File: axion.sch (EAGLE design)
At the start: 148 parts, among them IC1 3.3V, IC2 5V, Q2 12.288Mhz, U10 MIC2039, U11 WM8731, U2 Intel Edison, U4 FT232RLSSOP, U5 PCA9306D, U6 74HC4050, U7 TPA2005D1DGN, X1 MKDSN1,5/2-5,08, X2 ZX62R-AB-5P, X3 ST-005-G, X4 ZX62R-B-5P

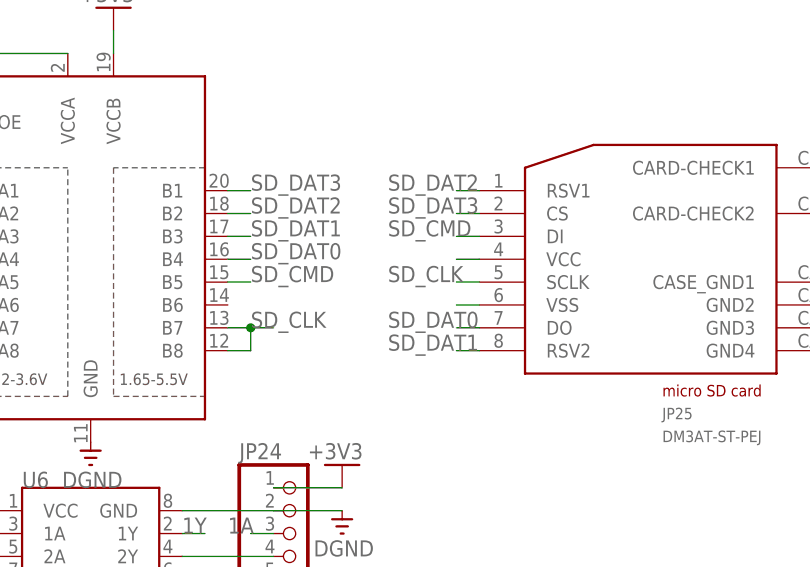
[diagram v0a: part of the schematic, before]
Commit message: Power microSD
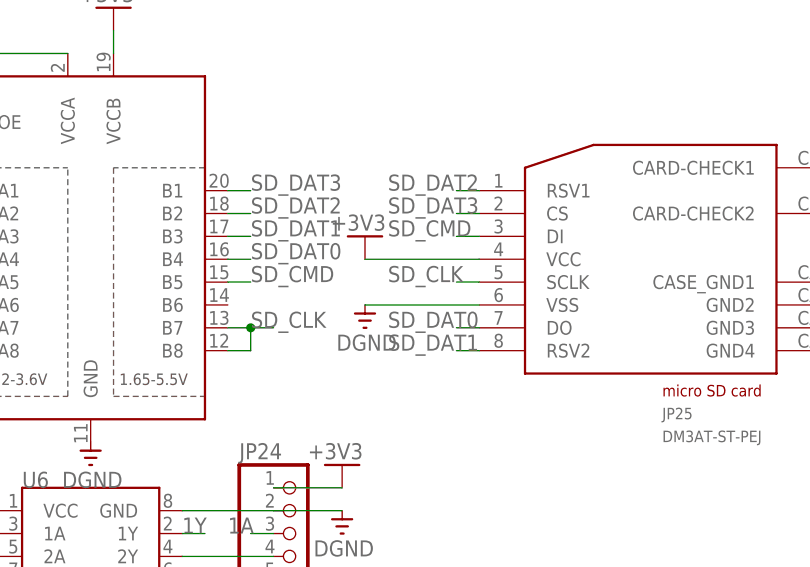
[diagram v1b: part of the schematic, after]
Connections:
- removed net N$49: JP25.VCC
- removed net N$51: JP25.VSS
- net +3V3: now also JP25.VCC
- net DGND: now also JP25.VSS
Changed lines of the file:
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@@
 </part>
 <part name="X4" library="hirose-zx" deviceset="ZX62R-B-5P" device=""/>
+<part name="DGND34" library="supply0" deviceset="DGND" device=""/>
+<part name="V43" library="supply0" deviceset="+3V3" device=""/>
 </parts>
 <sheets>
@@
 <instance part="X4" gate="C" x="-119.38" y="20.32" rot="MR0"/>
 <instance part="X4" gate="S" x="-124.46" y="10.16" rot="MR0"/>
+<instance part="DGND34" gate="G$1" x="78.74" y="-17.78"/>
+<instance part="V43" gate="G$1" x="78.74" y="-7.62"/>
 </instances>
 <busses>
@@
 <pinref part="DGND26" gate="G$1" pin="DGND"/>
 </segment>
+<segment>
+<pinref part="JP25" gate="G$1" pin="VSS"/>
+<pinref part="DGND34" gate="G$1" pin="DGND"/>
+<wire x1="91.44" y1="-15.24" x2="78.74" y2="-15.24" width="0.1524" layer="91"/>
+</segment>
 </net>
 <net name="+3V3" class="2">
@@
 <wire x1="-111.76" y1="50.8" x2="-116.84" y2="50.8" width="0.1524" layer="91"/>
 </segment>
+<segment>
+<pinref part="JP25" gate="G$1" pin="VCC"/>
+<pinref part="V43" gate="G$1" pin="+3V3"/>
+<wire x1="78.74" y1="-10.16" x2="91.44" y2="-10.16" width="0.1524" layer="91"/>
+</segment>
 </net>
 <net name="+5V" class="2">
@@
 </segment>
 </net>
-<net name="N$49" class="0">
-<segment>
-<pinref part="JP25" gate="G$1" pin="VCC"/>
-<wire x1="91.44" y1="-10.16" x2="88.9" y2="-10.16" width="0.1524" layer="91"/>
-</segment>
-</net>
-<net name="N$51" class="0">
-<segment>
-<pinref part="JP25" gate="G$1" pin="VSS"/>
-<wire x1="91.44" y1="-15.24" x2="88.9" y2="-15.24" width="0.1524" layer="91"/>
-</segment>
-</net>

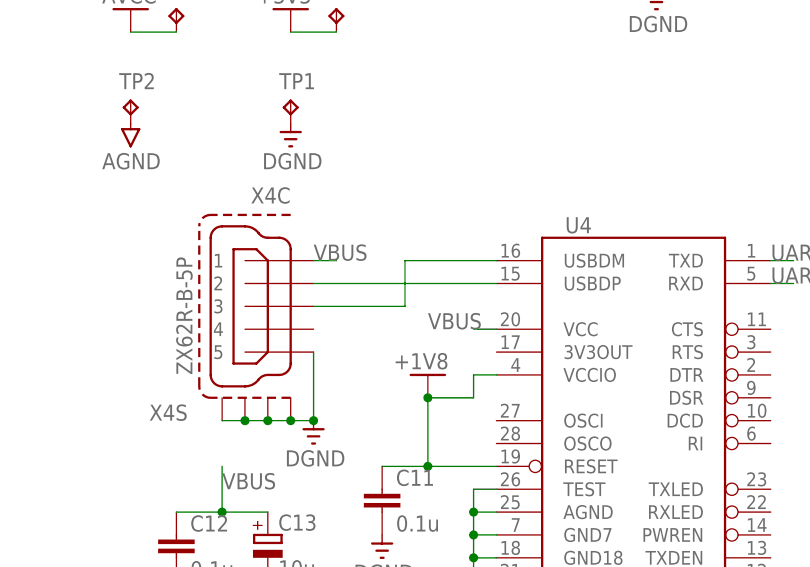
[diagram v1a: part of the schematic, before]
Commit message: Disconnect between USBD{P,M} of USB-serial bridge
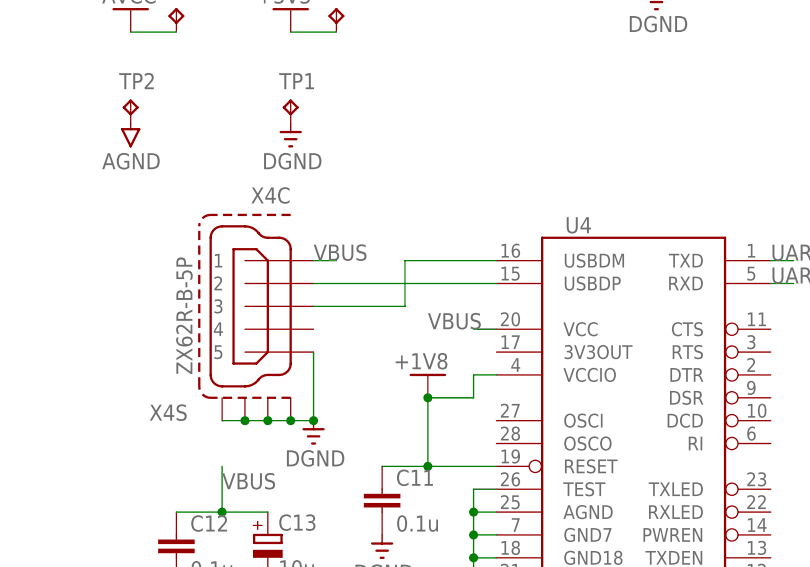
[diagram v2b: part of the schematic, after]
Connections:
- new net N$49: U4.USBDM, X4C.3
- net N$8: no longer U4.USBDM, X4C.3
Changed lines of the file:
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@@
-</segment>
-</net>
-<net name="N$8" class="0">
-<segment>
-<pinref part="U4" gate="G$1" pin="USBDP"/>
-<wire x1="-114.3" y1="22.86" x2="-104.14" y2="22.86" width="0.1524" layer="91"/>
-<wire x1="-104.14" y1="22.86" x2="-93.98" y2="22.86" width="0.1524" layer="91"/>
-<wire x1="-114.3" y1="20.32" x2="-104.14" y2="20.32" width="0.1524" layer="91"/>
-<wire x1="-104.14" y1="20.32" x2="-104.14" y2="22.86" width="0.1524" layer="91"/>
-<wire x1="-104.14" y1="22.86" x2="-104.14" y2="25.4" width="0.1524" layer="91"/>
-<pinref part="U4" gate="G$1" pin="USBDM"/>
-<wire x1="-104.14" y1="25.4" x2="-93.98" y2="25.4" width="0.1524" layer="91"/>
-<pinref part="X4" gate="C" pin="2"/>
-<pinref part="X4" gate="C" pin="3"/>
 </segment>
 </net>
@@
 </segment>
 </net>
+<net name="N$8" class="0">
+<segment>
+<pinref part="X4" gate="C" pin="2"/>
+<pinref part="U4" gate="G$1" pin="USBDP"/>
+<wire x1="-114.3" y1="22.86" x2="-93.98" y2="22.86" width="0.1524" layer="91"/>
+</segment>
+</net>
+<net name="N$49" class="0">
+<segment>
+<pinref part="U4" gate="G$1" pin="USBDM"/>
+<wire x1="-93.98" y1="25.4" x2="-104.14" y2="25.4" width="0.1524" layer="91"/>
+<wire x1="-104.14" y1="25.4" x2="-104.14" y2="20.32" width="0.1524" layer="91"/>
+<pinref part="X4" gate="C" pin="3"/>
+<wire x1="-104.14" y1="20.32" x2="-114.3" y2="20.32" width="0.1524" layer="91"/>
+</segment>
+</net>

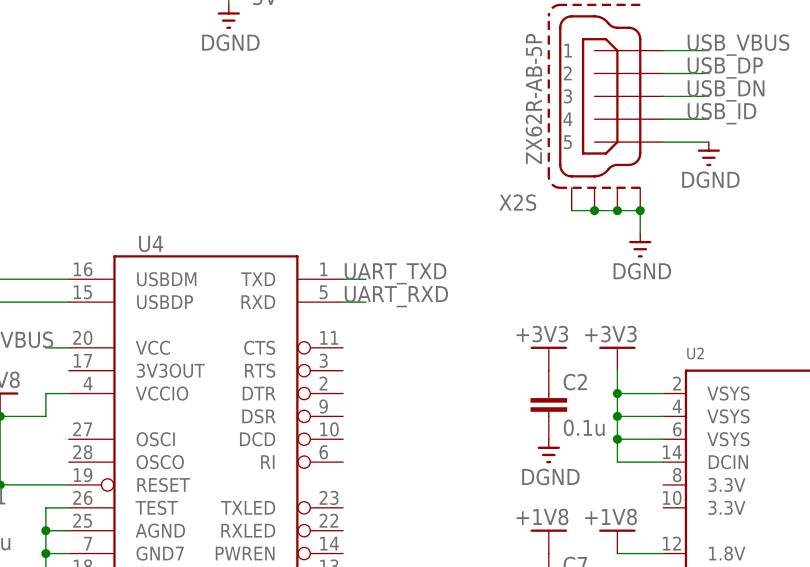
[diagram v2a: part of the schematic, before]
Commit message: Fix the order of {T,R}XD of serial
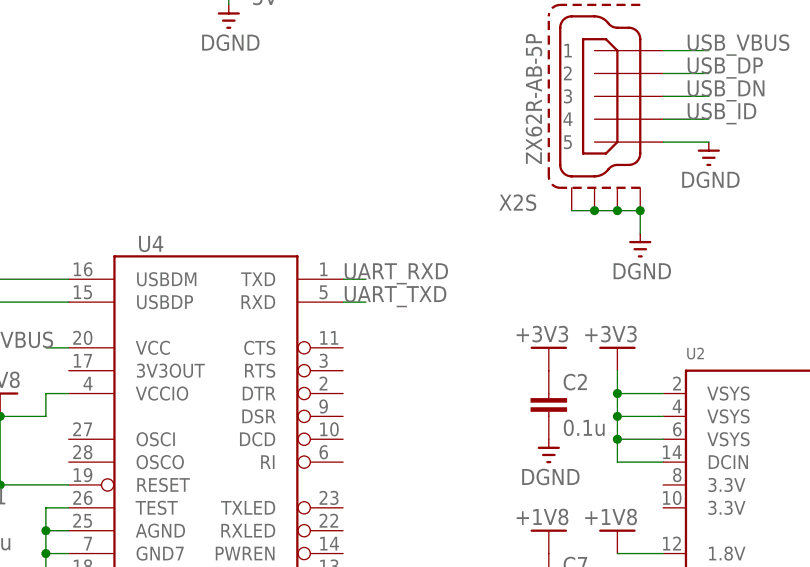
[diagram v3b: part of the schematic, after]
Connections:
- net UART_RXD: now also U4.TXD; no longer U4.RXD
- net UART_TXD: now also U4.RXD; no longer U4.TXD
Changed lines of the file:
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@@
 </segment>
 <segment>
-<pinref part="U4" gate="G$1" pin="TXD"/>
-<wire x1="-63.5" y1="25.4" x2="-60.96" y2="25.4" width="0.1524" layer="91"/>
-<label x="-63.5" y="25.4" size="1.778" layer="95"/>
+<pinref part="U4" gate="G$1" pin="RXD"/>
+<wire x1="-63.5" y1="22.86" x2="-60.96" y2="22.86" width="0.1524" layer="91"/>
+<label x="-63.5" y="22.86" size="1.778" layer="95"/>
 </segment>
 </net>
@@
 </segment>
 <segment>
-<pinref part="U4" gate="G$1" pin="RXD"/>
-<wire x1="-63.5" y1="22.86" x2="-60.96" y2="22.86" width="0.1524" layer="91"/>
-<label x="-63.5" y="22.86" size="1.778" layer="95"/>
+<pinref part="U4" gate="G$1" pin="TXD"/>
+<wire x1="-63.5" y1="25.4" x2="-60.96" y2="25.4" width="0.1524" layer="91"/>
+<label x="-63.5" y="25.4" size="1.778" layer="95"/>
 </segment>
 </net>

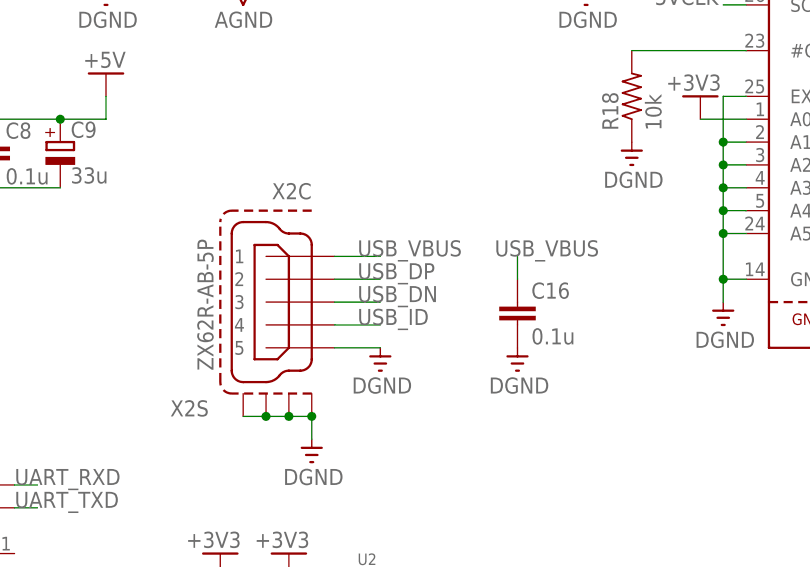
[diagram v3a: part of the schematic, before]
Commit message: Fix the order of USBD{P,M} od OTG USB
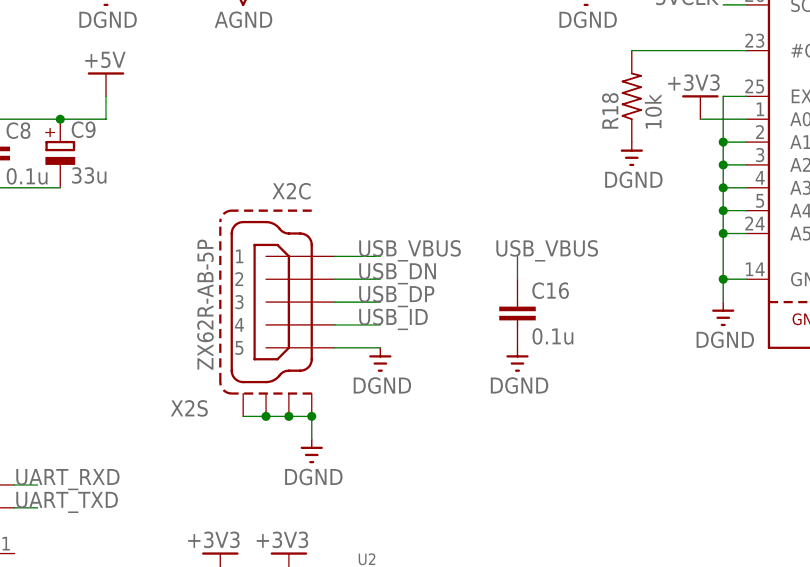
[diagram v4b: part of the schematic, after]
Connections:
- net USB_DN: now also X2C.2; no longer X2C.3
- net USB_DP: now also X2C.3; no longer X2C.2
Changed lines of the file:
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@@
 </segment>
 <segment>
-<wire x1="-27.94" y1="48.26" x2="-22.86" y2="48.26" width="0.1524" layer="91"/>
-<label x="-25.4" y="48.26" size="1.778" layer="95"/>
-<pinref part="X2" gate="C" pin="2"/>
+<wire x1="-27.94" y1="45.72" x2="-22.86" y2="45.72" width="0.1524" layer="91"/>
+<label x="-25.4" y="45.72" size="1.778" layer="95"/>
+<pinref part="X2" gate="C" pin="3"/>
 </segment>
 </net>
@@
 </segment>
 <segment>
-<wire x1="-27.94" y1="45.72" x2="-22.86" y2="45.72" width="0.1524" layer="91"/>
-<label x="-25.4" y="45.72" size="1.778" layer="95"/>
-<pinref part="X2" gate="C" pin="3"/>
+<wire x1="-27.94" y1="48.26" x2="-22.86" y2="48.26" width="0.1524" layer="91"/>
+<label x="-25.4" y="48.26" size="1.778" layer="95"/>
+<pinref part="X2" gate="C" pin="2"/>
 </segment>
 </net>

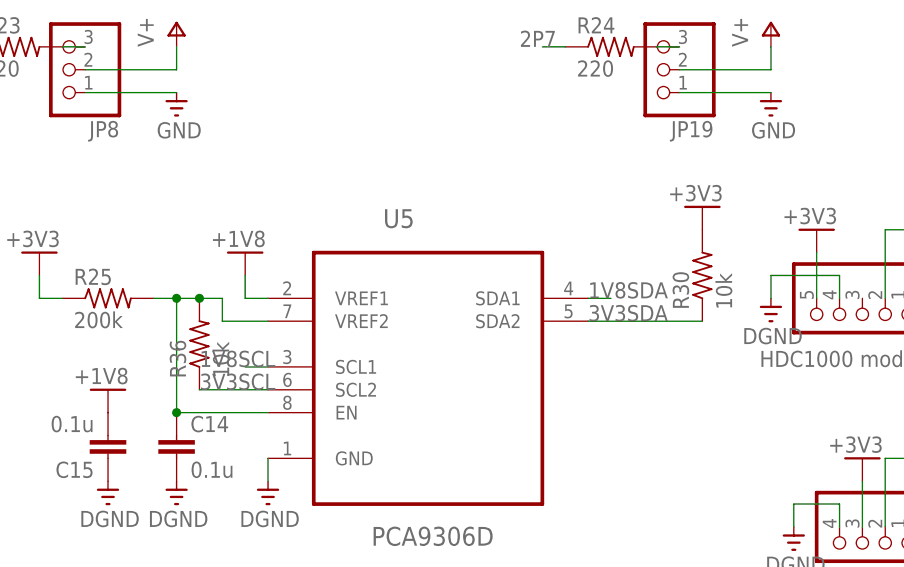
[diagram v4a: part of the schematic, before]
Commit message: Remove 10k pullup of I2C
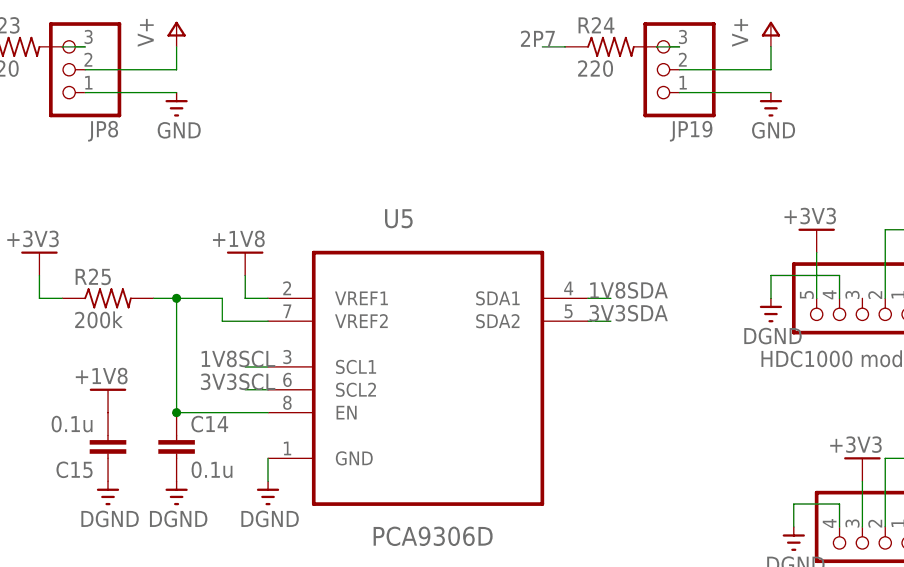
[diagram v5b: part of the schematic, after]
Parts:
- removed R30, R36: 10k, resistor:R-US_M1206
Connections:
- net +3V3: no longer R30.2
- net 3V3SCL: no longer R36.1
- net 3V3SDA: no longer R30.1
- net N$10: no longer R36.2
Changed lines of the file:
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@@
 <part name="R26" library="resistor" deviceset="R-US_" device="R0603" value="47k"/>
 <part name="AGND8" library="supply0" deviceset="AGND" device=""/>
-<part name="R30" library="resistor" deviceset="R-US_" device="M1206" value="10k"/>
-<part name="R36" library="resistor" deviceset="R-US_" device="M1206" value="10k"/>
-<part name="V25" library="supply0" deviceset="+3V3" device=""/>
 <part name="JP27" library="pinhead" deviceset="PINHD-1X2" device="" value="PCTRL"/>
 <part name="R37" library="resistor" deviceset="R-US_" device="M1206" value="10k"/>
@@
 <instance part="R26" gate="G$1" x="53.34" y="-129.54" rot="R270"/>
 <instance part="AGND8" gate="VR1" x="53.34" y="-137.16"/>
-<instance part="R30" gate="G$1" x="231.14" y="-66.04" rot="R90"/>
-<instance part="R36" gate="G$1" x="175.26" y="-73.66" rot="R90"/>
-<instance part="V25" gate="G$1" x="231.14" y="-58.42"/>
 <instance part="JP27" gate="G$1" x="147.32" y="-93.98"/>
 <instance part="R37" gate="G$1" x="139.7" y="-86.36" rot="R90"/>
@@
 </segment>
 <segment>
-<pinref part="R30" gate="G$1" pin="2"/>
-<pinref part="V25" gate="G$1" pin="+3V3"/>
-</segment>
-<segment>
 <pinref part="R37" gate="G$1" pin="2"/>
 <pinref part="V26" gate="G$1" pin="+3V3"/>
@@
 <pinref part="U5" gate="A" pin="SDA2"/>
 <label x="218.44" y="-71.12" size="1.778" layer="95"/>
-<pinref part="R30" gate="G$1" pin="1"/>
-<wire x1="218.44" y1="-71.12" x2="231.14" y2="-71.12" width="0.1524" layer="91"/>
+<wire x1="218.44" y1="-71.12" x2="220.98" y2="-71.12" width="0.1524" layer="91"/>
 </segment>
 <segment>
@@
 <pinref part="U5" gate="A" pin="SCL2"/>
 <label x="175.26" y="-78.74" size="1.778" layer="95"/>
-<pinref part="R36" gate="G$1" pin="1"/>
-<wire x1="182.88" y1="-78.74" x2="175.26" y2="-78.74" width="0.1524" layer="91"/>
+<wire x1="182.88" y1="-78.74" x2="180.34" y2="-78.74" width="0.1524" layer="91"/>
 </segment>
 <segment>
@@
 <wire x1="182.88" y1="-71.12" x2="177.8" y2="-71.12" width="0.1524" layer="91"/>
 <wire x1="177.8" y1="-71.12" x2="177.8" y2="-68.58" width="0.1524" layer="91"/>
-<wire x1="177.8" y1="-68.58" x2="175.26" y2="-68.58" width="0.1524" layer="91"/>
-<pinref part="R36" gate="G$1" pin="2"/>
-<junction x="175.26" y="-68.58"/>
-<wire x1="175.26" y1="-68.58" x2="172.72" y2="-68.58" width="0.1524" layer="91"/>
+<wire x1="177.8" y1="-68.58" x2="172.72" y2="-68.58" width="0.1524" layer="91"/>
 <junction x="172.72" y="-68.58"/>
 </segment>
